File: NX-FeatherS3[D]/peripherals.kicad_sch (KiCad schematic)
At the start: 28 parts, among them SW1 SW_Push, SW2 SW_Push, U10 BNO085, U3 MAX17048G_T10, U9 MAX98357A, Y2 32.768

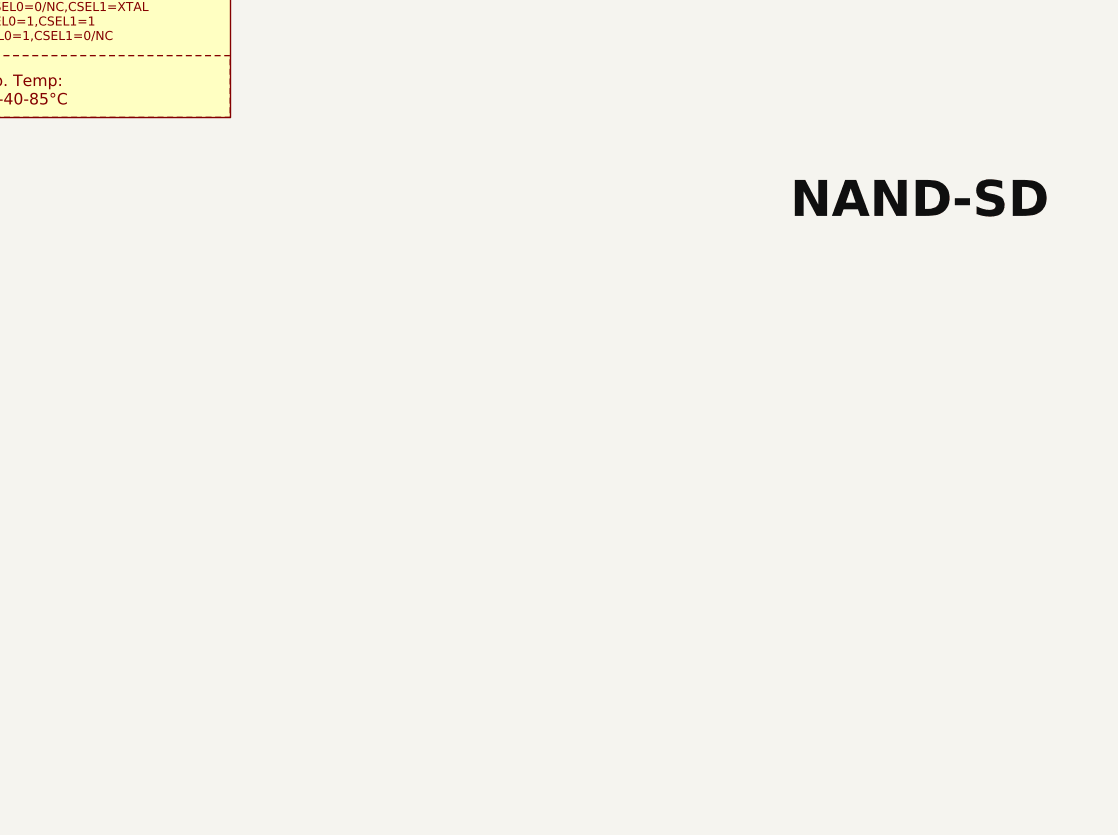
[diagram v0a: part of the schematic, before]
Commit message: Added v1p0, updated Version
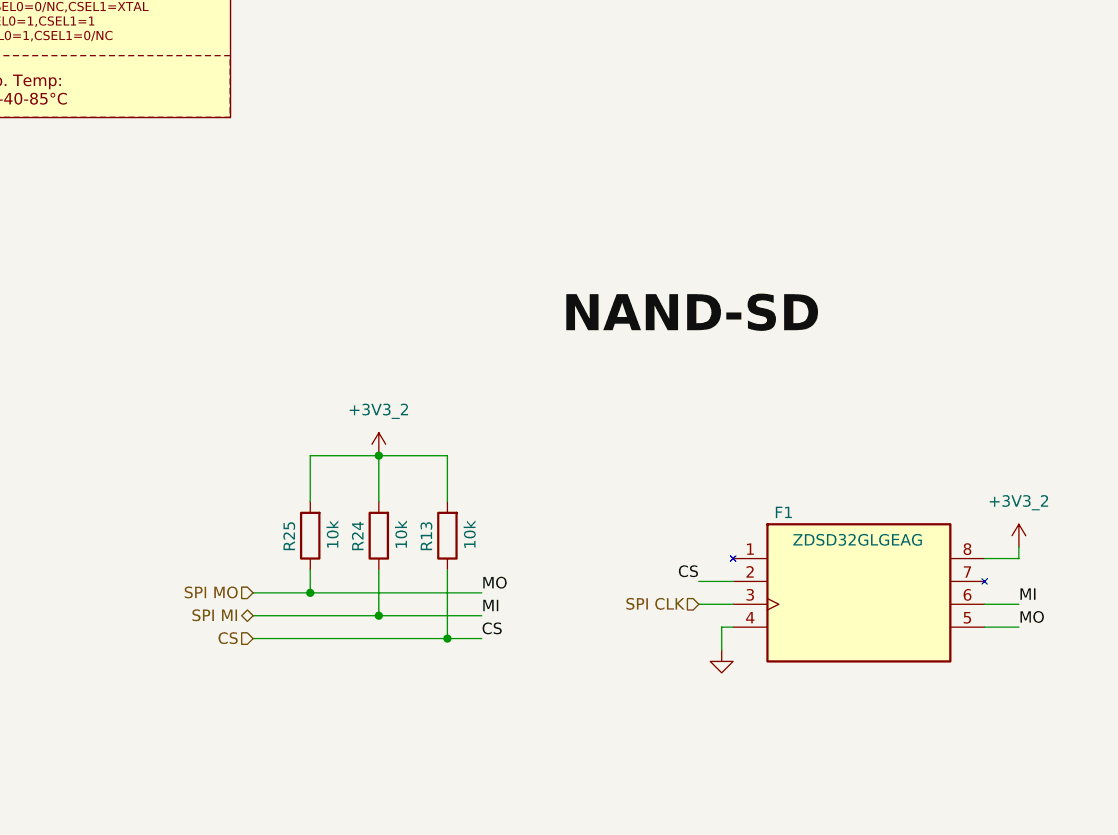
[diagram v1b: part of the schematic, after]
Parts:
- added F1: ZDSD32GLGEAG, Package_LGA:LGA-8_8x6.2mm_P1.27mm, symbol Connector_Generic:Conn_01x08
- added R13, R24, R25: 10k, symbol Device:R
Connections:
- net +3V3_2: now also F1.8 (VDD), R13.2, R24.2, R25.2
- net GND: now also F1.4 (GND)
- new net CS: F1.2 (SD3/CS#), R13.1
- new net SPI CLK: F1.3 (CLK)
- new net SPI MI: F1.6 (SD0/DO), R24.1
- new net SPI MO: F1.5 (CMD/DI), R25.1
